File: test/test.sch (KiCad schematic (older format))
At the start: 2 parts

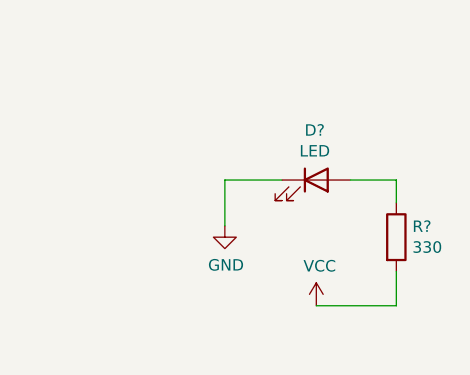
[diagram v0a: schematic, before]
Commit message: eliminó R2
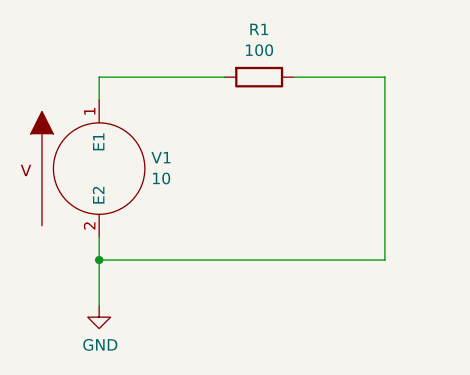
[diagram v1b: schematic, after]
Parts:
- removed D?: LED, symbol Device:LED
- removed R?: 330, symbol Device:R
- added R1: 100, symbol Device:R
- added V1: 10, symbol pspice:VSOURCE
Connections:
- net GND: now also R1.1, V1.2 (E2)
- new net: R1.2, V1.1 (E1)
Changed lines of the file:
@@
 $EndDescr
 $Comp
-L Device:R R?
-U 1 1 5FFC580C
-P 3100 2500
-F 0 "R?" H 3170 2546 50  0000 L CNN
-F 1 "330" H 3170 2455 50  0000 L CNN
-F 2 "" V 3030 2500 50  0001 C CNN
-F 3 "~" H 3100 2500 50  0001 C CNN
-	1    3100 2500
+L pspice:VSOURCE V1
+U 1 1 5FFD45F7
+P 1800 2200
+F 0 "V1" H 2028 2246 50  0000 L CNN
+F 1 "10" H 2028 2155 50  0000 L CNN
+F 2 "" H 1800 2200 50  0001 C CNN
+F 3 "~" H 1800 2200 50  0001 C CNN
+	1    1800 2200
 	1    0    0    -1
 $EndComp
 $Comp
-L Device:LED D?
-U 1 1 5FFC6305
-P 2750 2250
-F 0 "D?" H 2743 2467 50  0000 C CNN
-F 1 "LED" H 2743 2376 50  0000 C CNN
-F 2 "" H 2750 2250 50  0001 C CNN
-F 3 "~" H 2750 2250 50  0001 C CNN
-	1    2750 2250
-	1    0    0    -1
+L Device:R R1
+U 1 1 5FFD4A0B
+P 2500 1800
+F 0 "R1" V 2293 1800 50  0000 C CNN
+F 1 "100" V 2384 1800 50  0000 C CNN
+F 2 "" V 2430 1800 50  0001 C CNN
+F 3 "~" H 2500 1800 50  0001 C CNN
+	1    2500 1800
+	0    1    1    0
 $EndComp
 $Comp
-L power:VCC #PWR0101
-U 1 1 5FFC881F
-P 2750 2800
-F 0 "#PWR0101" H 2750 2650 50  0001 C CNN
-F 1 "VCC" H 2765 2973 50  0000 C CNN
-F 2 "" H 2750 2800 50  0001 C CNN
-F 3 "" H 2750 2800 50  0001 C CNN
-	1    2750 2800
-	1    0    0    -1
-$EndComp
-$Comp
-L power:GND #PWR0102
-U 1 1 5FFC8E35
-P 2350 2450
-F 0 "#PWR0102" H 2350 2200 50  0001 C CNN
-F 1 "GND" H 2355 2277 50  0000 C CNN
-F 2 "" H 2350 2450 50  0001 C CNN
-F 3 "" H 2350 2450 50  0001 C CNN
-	1    2350 2450
+L power:GND #PWR?
+U 1 1 5FFD5A07
+P 1800 2800
+F 0 "#PWR?" H 1800 2550 50  0001 C CNN
+F 1 "GND" H 1805 2627 50  0000 C CNN
+F 2 "" H 1800 2800 50  0001 C CNN
+F 3 "" H 1800 2800 50  0001 C CNN
+	1    1800 2800
 	1    0    0    -1
 $EndComp
 Wire Wire Line
-	3100 2350 3100 2250
+	1800 1900 1800 1800
 Wire Wire Line
-	3100 2250 2900 2250
+	1800 1800 2350 1800
 Wire Wire Line
-	2600 2250 2350 2250
+	2650 1800 3050 1800
 Wire Wire Line
-	2350 2250 2350 2450
+	1800 2500 1800 2600
 Wire Wire Line
-	2750 2800 3100 2800
+	3050 2600 1800 2600
+Connection ~ 1800 2600
 Wire Wire Line
-	3100 2800 3100 2650
+	1800 2600 1800 2800
+Wire Wire Line
+	3050 1800 3050 2600
 $EndSCHEMATC

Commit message: led adicional
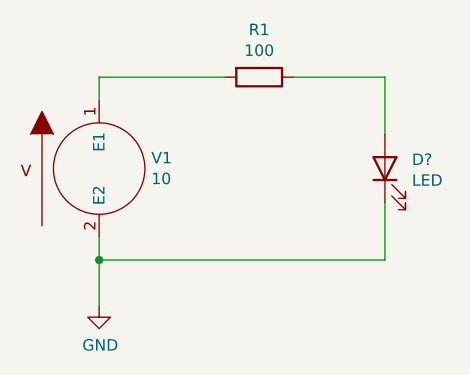
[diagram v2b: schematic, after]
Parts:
- added D?: LED, symbol Device:LED
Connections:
- net GND: now also D?.1 (K); no longer R1.1
- new net: D?.2 (A), R1.1
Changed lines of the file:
@@
 Wire Wire Line
 	1800 2600 1800 2800
+$Comp
+L Device:LED D?
+U 1 1 5FFBBDC1
+P 3050 2200
+F 0 "D?" V 3089 2082 50  0000 R CNN
+F 1 "LED" V 2998 2082 50  0000 R CNN
+F 2 "" H 3050 2200 50  0001 C CNN
+F 3 "~" H 3050 2200 50  0001 C CNN
+	1    3050 2200
+	0    -1   -1   0
+$EndComp
 Wire Wire Line
-	3050 1800 3050 2600
+	3050 1800 3050 2050
+Wire Wire Line
+	3050 2350 3050 2600
 $EndSCHEMATC

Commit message: prueba_led2
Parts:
- D01: renamed from D?; Spice_Model (none) -> LED; Spice_Netlist_Enabled (none) -> Y; Spice_Node_Sequence (none) -> 2 1; Spice_Primitive (none) -> D
- R1: value 100 -> 2k
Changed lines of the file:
@@
 P 2500 1800
 F 0 "R1" V 2293 1800 50  0000 C CNN
-F 1 "100" V 2384 1800 50  0000 C CNN
+F 1 "2k" V 2384 1800 50  0000 C CNN
 F 2 "" V 2430 1800 50  0001 C CNN
 F 3 "~" H 2500 1800 50  0001 C CNN
@@
 	1800 2600 1800 2800
 $Comp
-L Device:LED D?
+L Device:LED D01
 U 1 1 5FFBBDC1
 P 3050 2200
-F 0 "D?" V 3089 2082 50  0000 R CNN
+F 0 "D01" V 3089 2082 50  0000 R CNN
 F 1 "LED" V 2998 2082 50  0000 R CNN
 F 2 "" H 3050 2200 50  0001 C CNN
 F 3 "~" H 3050 2200 50  0001 C CNN
+F 4 "D" H 3050 2200 50  0001 C CNN "Spice_Primitive"
+F 5 "LED" H 3050 2200 50  0001 C CNN "Spice_Model"
+F 6 "Y" H 3050 2200 50  0001 C CNN "Spice_Netlist_Enabled"
+F 7 "2 1" H 3050 2200 50  0001 C CNN "Spice_Node_Sequence"
 	1    3050 2200
 	0    -1   -1   0

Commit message: resistencia 1k
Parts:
- R1: value 2k -> 1k
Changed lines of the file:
@@
 P 2500 1800
 F 0 "R1" V 2293 1800 50  0000 C CNN
-F 1 "2k" V 2384 1800 50  0000 C CNN
+F 1 "1k" V 2384 1800 50  0000 C CNN
 F 2 "" V 2430 1800 50  0001 C CNN
 F 3 "~" H 2500 1800 50  0001 C CNN

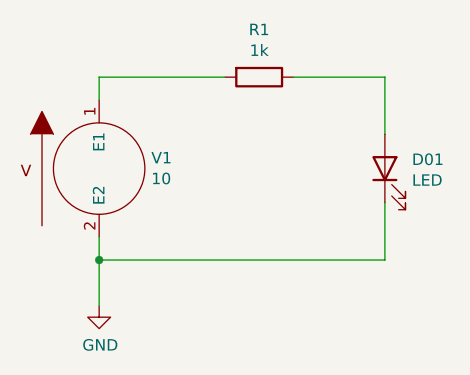
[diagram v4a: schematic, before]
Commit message: cambio resistencia
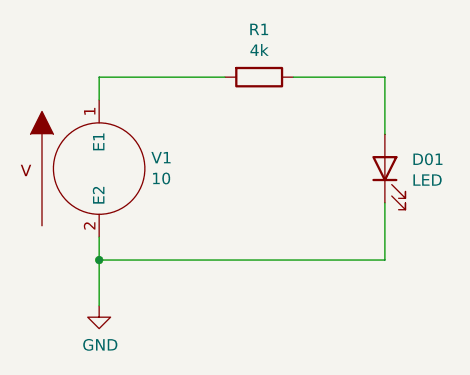
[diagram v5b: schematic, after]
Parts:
- R1: value 1k -> 4k
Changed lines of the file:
@@
 P 2500 1800
 F 0 "R1" V 2293 1800 50  0000 C CNN
-F 1 "1k" V 2384 1800 50  0000 C CNN
+F 1 "4k" V 2384 1800 50  0000 C CNN
 F 2 "" V 2430 1800 50  0001 C CNN
 F 3 "~" H 2500 1800 50  0001 C CNN

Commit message: Agregue libreria de LED
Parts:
- D01: Spice_Model LED -> (none); Spice_Primitive D -> I
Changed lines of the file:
@@
 F 2 "" H 3050 2200 50  0001 C CNN
 F 3 "~" H 3050 2200 50  0001 C CNN
-F 4 "D" H 3050 2200 50  0001 C CNN "Spice_Primitive"
-F 5 "LED" H 3050 2200 50  0001 C CNN "Spice_Model"
-F 6 "Y" H 3050 2200 50  0001 C CNN "Spice_Netlist_Enabled"
-F 7 "2 1" H 3050 2200 50  0001 C CNN "Spice_Node_Sequence"
+F 4 "I" H 3050 2200 50  0001 C CNN "Spice_Primitive"
+F 5 "Y" H 3050 2200 50  0001 C CNN "Spice_Netlist_Enabled"
+F 6 "2 1" H 3050 2200 50  0001 C CNN "Spice_Node_Sequence"
 	1    3050 2200
 	0    -1   -1   0
